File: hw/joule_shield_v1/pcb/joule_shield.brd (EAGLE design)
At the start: 60 x 40 mm, 143 parts, among them J1 MF-CON-MICROUSB-RIGHT, J4 USB_AUSB_A_SMT_RA, J5 JST-ZH5SMT_RA, J6 INTEL_JOULE_J6, J7 INTEL_JOULE_J7, J8 DM3ATDM3AT, Q1 NFETEMT3F, Q2 NFETEMT3F, Q3 NFETEMT3F, Q4 NFETEMT3F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

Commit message: Route power of BQ25892.
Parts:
- moved F1 1.43 mm to (45.4, 36.3)
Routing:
- net VIN_CHRG: track 0.00 -> 7.46 mm
- net N$12: track 0.00 -> 5.69 mm
- net VSYS: track 0.00 -> 4.13 mm, vias 0 -> 3
- net N$11: track 0.00 -> 3.97 mm
- net N$3: track 0.00 -> 2.97 mm
- net N$4: track 0.00 -> 2.58 mm
- net N$9: track 0.00 -> 1.90 mm
- net VREGN: track 0.00 -> 1.78 mm
- net GND: track 0.00 -> 1.72 mm, vias 0 -> 8
- net N$2: track 0.00 -> 1.72 mm
- net N$5: track 0.00 -> 1.60 mm
- added copper zone on layer 16, net GND
- added copper zone on layer 16, net VSYS

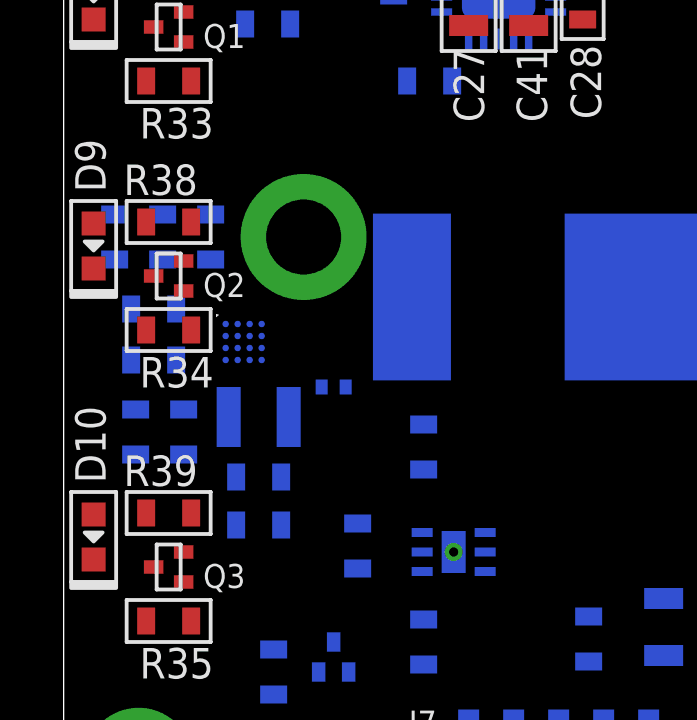
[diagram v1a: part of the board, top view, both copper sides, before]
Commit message: joule shield: ground and power layout for FAN48623
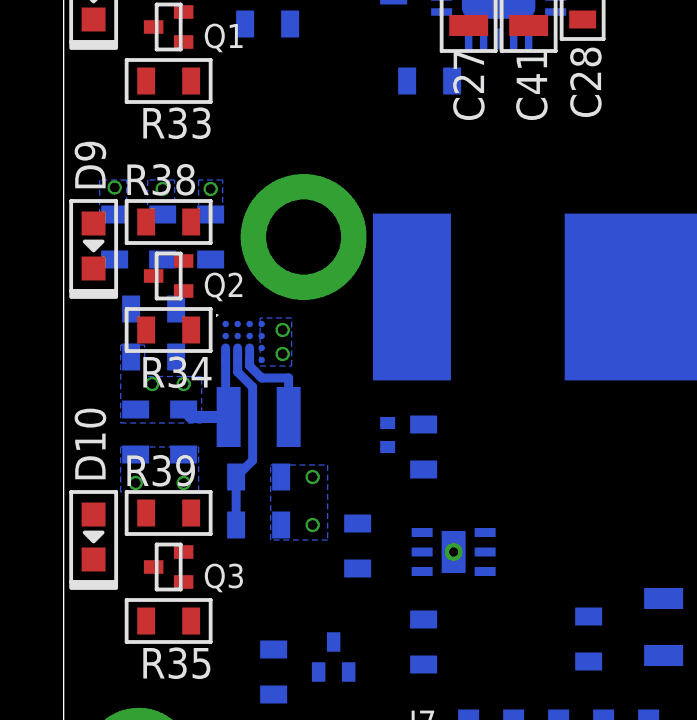
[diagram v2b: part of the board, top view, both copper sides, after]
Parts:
- moved D3 2.41 mm to (10.8, 15.4), turned to 90 degrees
- moved R12 0.10 mm to (3.00, 18.0)
- turned R10 to 90 degrees
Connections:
- net V5P0V: no longer R12.P$1, R37.P$1, R38.P$1, R39.P$1
- net VSYS: now also R12.P$1, R37.P$1, R38.P$1, R39.P$1
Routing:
- net V5P0V: track 0.00 -> 6.33 mm
- net VSYS: track 4.13 -> 8.07 mm, vias 3 -> 7
- net N$13: track 0.00 -> 3.37 mm
- net GND: vias 8 -> 15

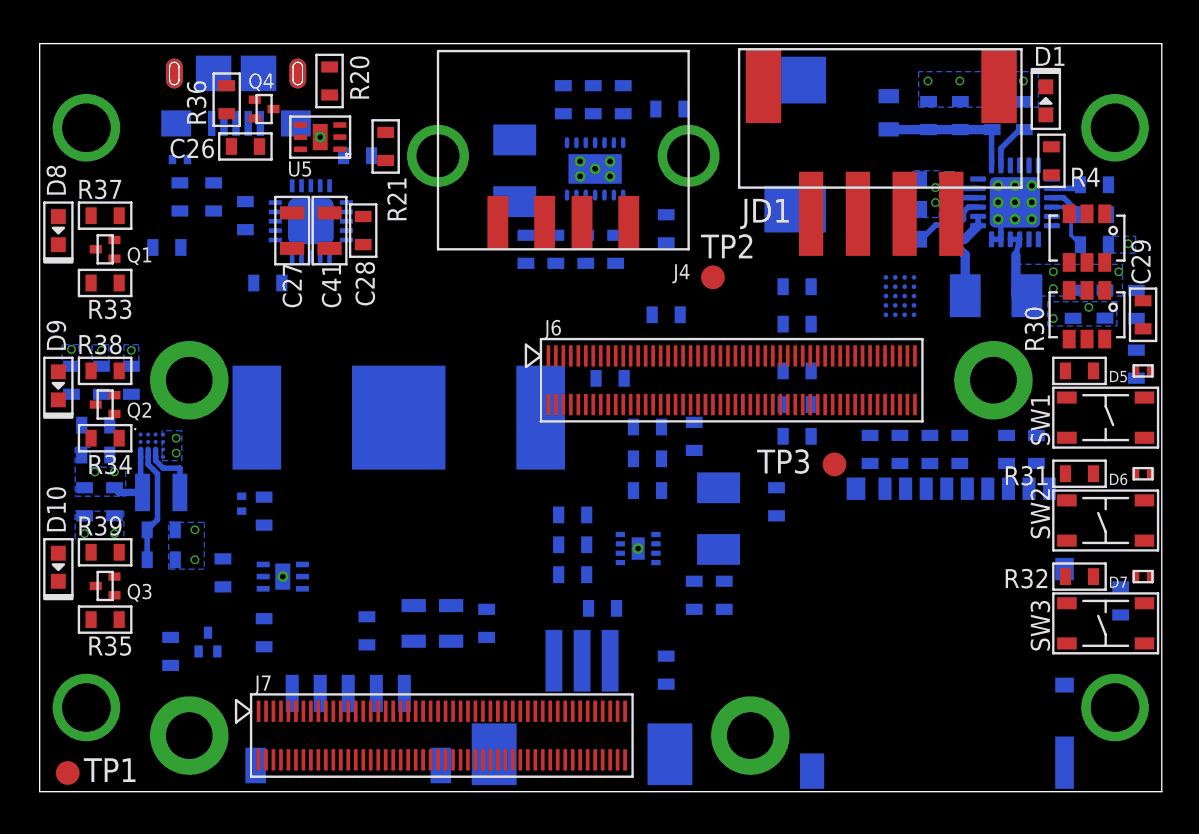
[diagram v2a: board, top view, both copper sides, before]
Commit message: joule shield: Draft USB routing.
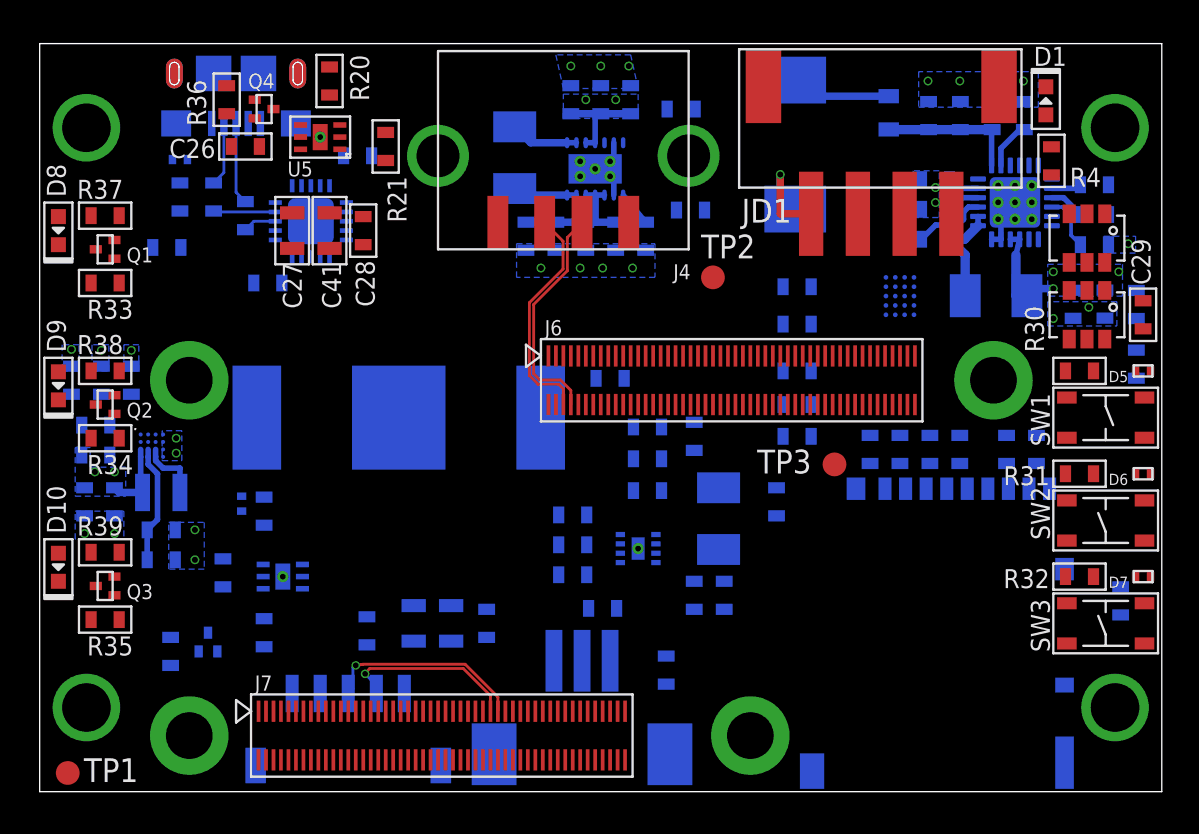
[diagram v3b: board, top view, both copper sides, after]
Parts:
- moved R14 5.75 mm to (34.8, 31.1), turned to 0 degrees
- moved C16 1.17 mm to (32.4, 29.7)
- moved C17 0.70 mm to (26.0, 29.7)
- moved C18 0.70 mm to (27.6, 29.7)
- moved C19 0.70 mm to (29.2, 29.7)
- moved C20 0.70 mm to (30.8, 29.7)
- moved L3 0.70 mm to (25.4, 33.9)
- moved R13 0.60 mm to (34.3, 36.5)
- moved C15 0.40 mm to (31.6, 37.0)
- moved C13 0.40 mm to (28.4, 37.0)
- moved C14 0.40 mm to (30.0, 37.0)
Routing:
- net USB2_0_P: track 0.00 -> 12.3 mm
- net USB2_0_N: track 0.00 -> 12.3 mm
- net USB2_1_P: track 0.00 -> 10.8 mm, vias 0 -> 1
- net USB2_1_N: track 0.00 -> 9.75 mm, vias 0 -> 1
- net V3P3V: track 0.00 -> 7.25 mm
- net VSYS: track 8.07 -> 14.9 mm, vias 7 -> 9
- net N$28: track 0.00 -> 5.93 mm, vias 0 -> 1
- net N$31: track 0.00 -> 5.36 mm
- net N$48: track 0.00 -> 4.39 mm
- net N$16: track 0.00 -> 3.65 mm
- net N$17: track 0.00 -> 3.44 mm
- net N$50: track 0.00 -> 3.41 mm
- net N$39: track 0.00 -> 3.32 mm
- net GND: track 1.72 -> 4.12 mm, vias 15 -> 22
- net N$19: track 0.00 -> 1.88 mm
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
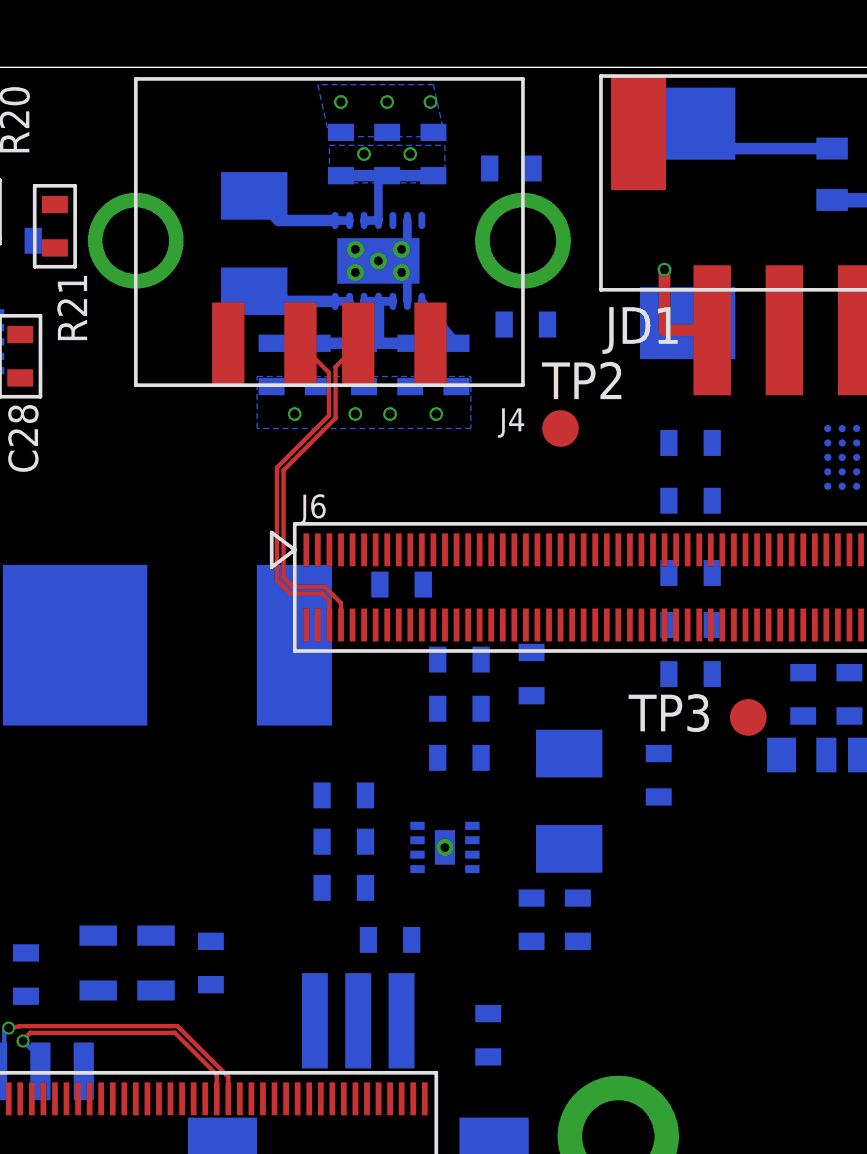
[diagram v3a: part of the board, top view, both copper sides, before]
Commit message: joule shield: Draft power routing for TLV62084.
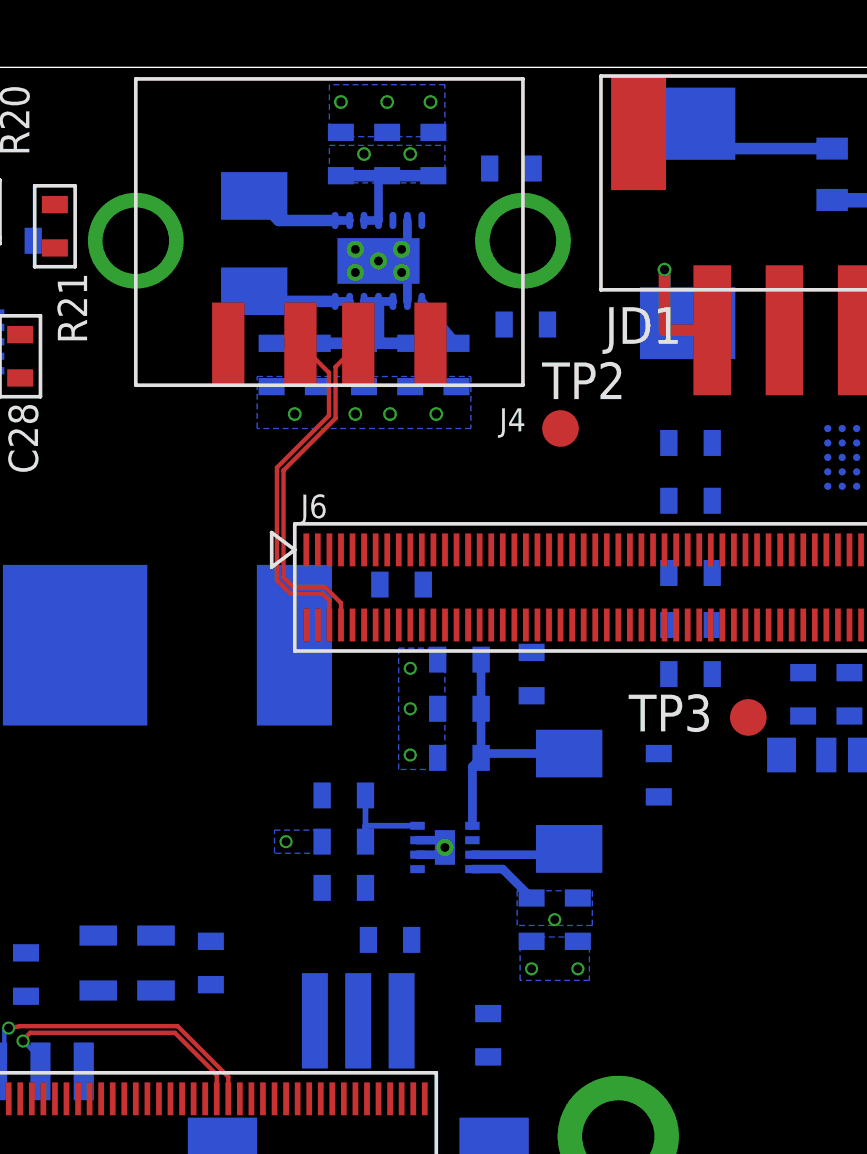
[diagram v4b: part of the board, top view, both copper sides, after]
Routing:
- net V1P8V: track 0.00 -> 8.99 mm
- net N$26: track 0.00 -> 3.95 mm
- net N$23: track 0.00 -> 3.43 mm
- net VSYS: track 14.9 -> 17.4 mm, vias 9 -> 10
- net GND: track 4.12 -> 6.23 mm, vias 22 -> 28

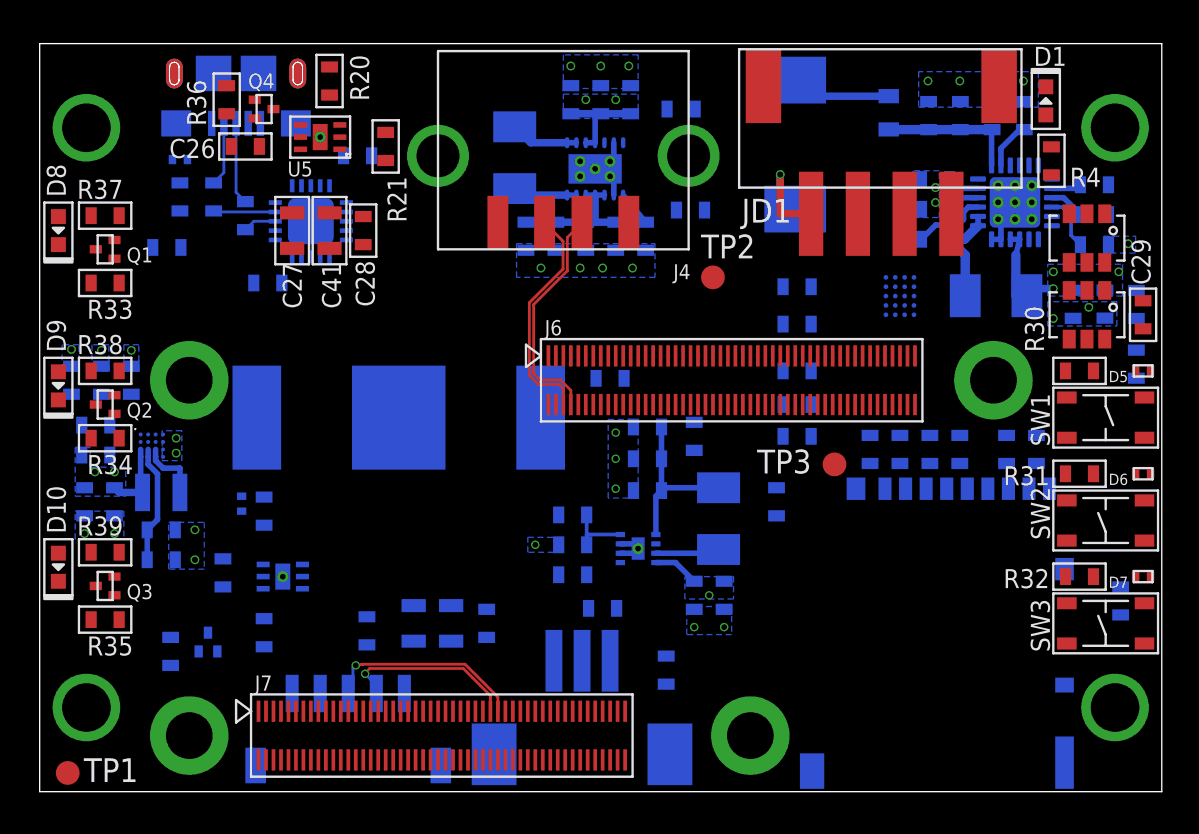
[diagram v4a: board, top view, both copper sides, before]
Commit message: joule shield: Route power for TPS2553s.
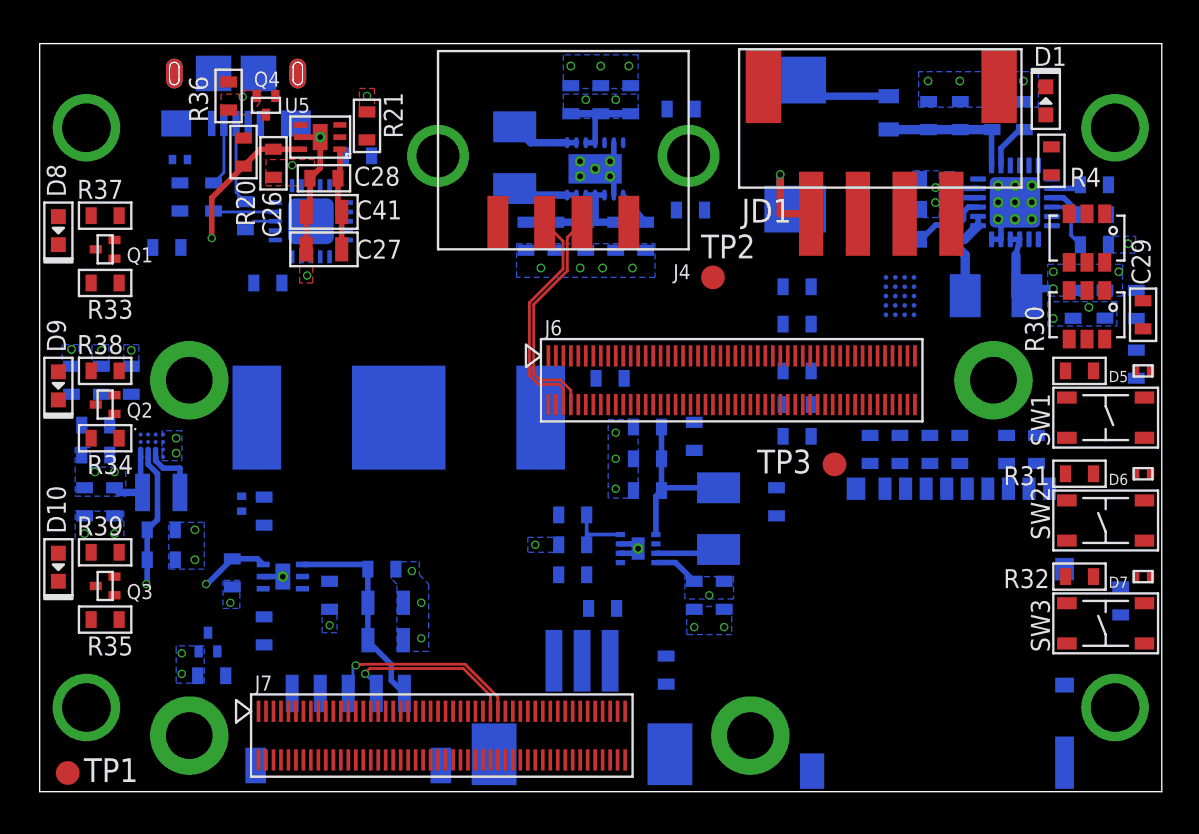
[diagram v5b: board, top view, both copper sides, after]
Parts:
- moved C32 6.31 mm to (18.3, 11.9), turned to 180 degrees
- moved R20 5.97 mm to (10.9, 34.2), turned to 90 degrees
- moved C42 3.67 mm to (18.5, 10.1), turned to 180 degrees
- moved C28 3.50 mm to (15.2, 32.8), turned to 180 degrees
- moved R24 2.76 mm to (15.5, 10.5)
- moved R40 2.56 mm to (9.20, 6.20), turned to 0 degrees
- moved C27 1.97 mm to (15.2, 29.0), turned to 180 degrees
- moved C31 1.75 mm to (18.5, 8.10), turned to 180 degrees
- moved C26 1.75 mm to (12.5, 33.6), turned to 270 degrees
- moved R21 1.49 mm to (17.5, 35.6), turned to 90 degrees
- moved C41 1.04 mm to (15.2, 31.0), turned to 180 degrees
- moved C30 0.50 mm to (10.3, 11.7)
- moved Q4 0.22 mm to (12.1, 36.7), turned to 180 degrees
- moved R36 0.22 mm to (10.1, 37.2)
- moved R23 0.10 mm to (12.0, 8.60)
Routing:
- net V5P0V: track 6.33 -> 42.5 mm, vias 0 -> 3
- net V5P0V_USBB: track 0.00 -> 11.2 mm
- net GND: track 6.23 -> 14.8 mm, vias 28 -> 39
- net V5P0V_USBA: track 0.00 -> 5.65 mm
- added copper zone on layer 1, net GND

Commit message: joule shield: Do grounds for things up through the SD level converter.
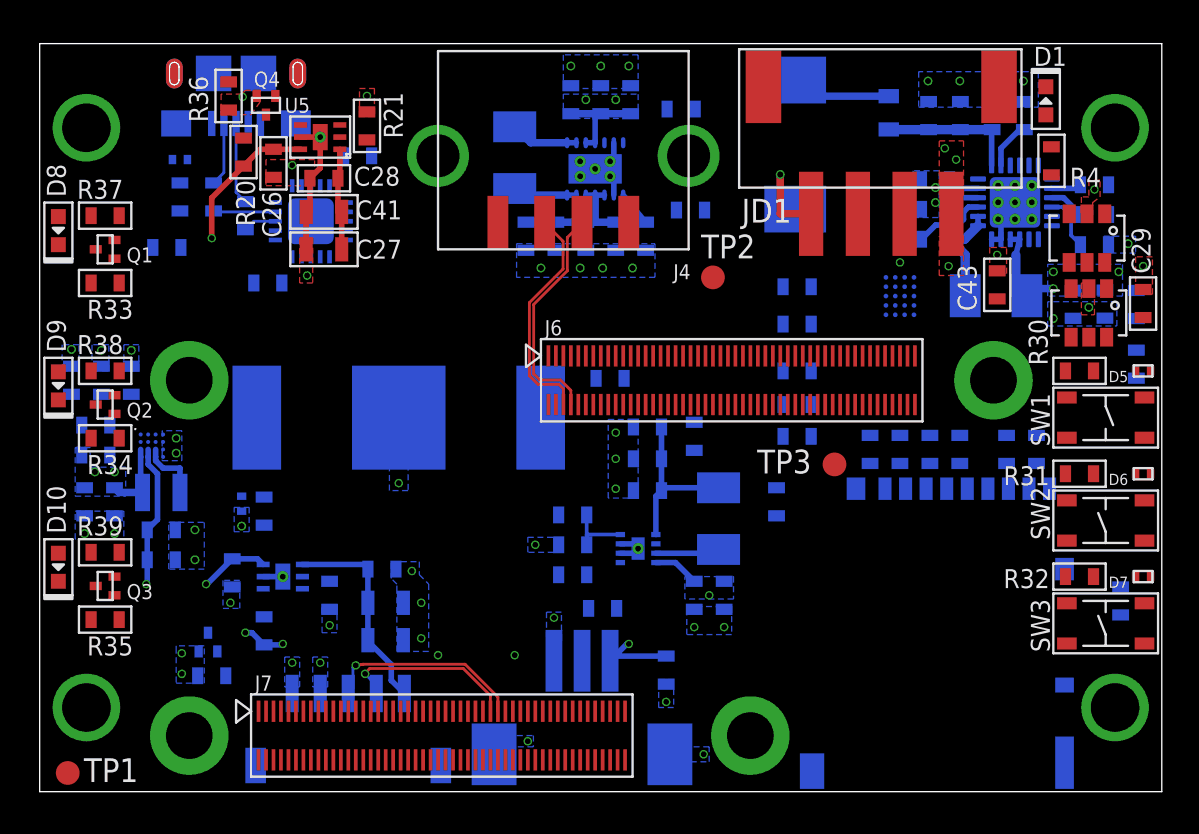
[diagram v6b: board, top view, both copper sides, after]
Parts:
- added C43: 0.1uF, mf_passives:C0603
- moved C29 0.60 mm to (59.0, 26.1)
- moved U8 0.14 mm to (56.1, 25.6)
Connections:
- net GND: now also C43.P$2
- net V5P0V: now also C43.P$1
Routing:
- net V5P0V: track 42.5 -> 72.2 mm, vias 3 -> 8
- net GND: vias 39 -> 54

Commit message: joule shield: power and ground for the joule connectors
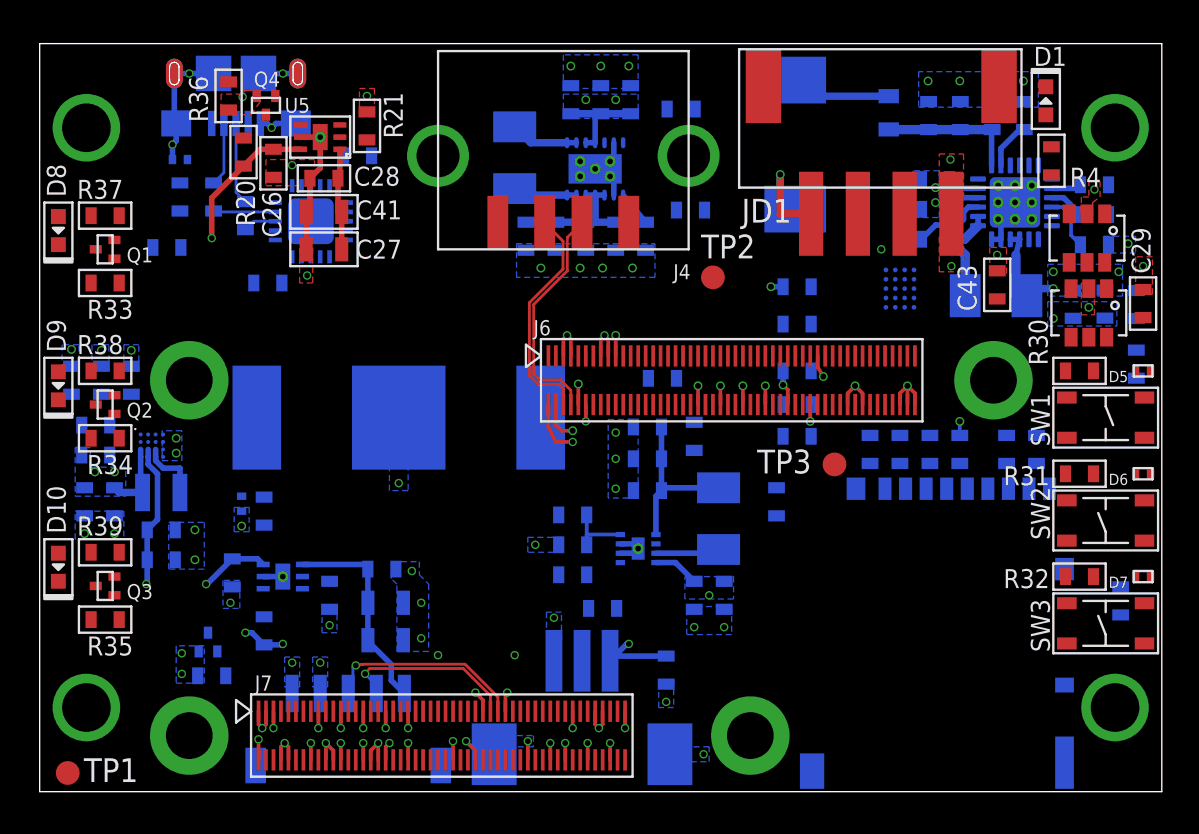
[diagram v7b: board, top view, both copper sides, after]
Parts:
- moved R22 2.80 mm to (33.3, 22.1), turned to 0 degrees
- moved U9 0.40 mm to (46.0, 26.9)
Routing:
- net GND: track 14.8 -> 72.8 mm, vias 54 -> 95
- net VSYS: track 17.4 -> 31.9 mm, vias 10 -> 17
